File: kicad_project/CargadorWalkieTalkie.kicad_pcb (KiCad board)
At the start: 2 copper layers, 9 parts, among them J1 Screw_Terminal_01x02, J2 Screw_Terminal_01x02

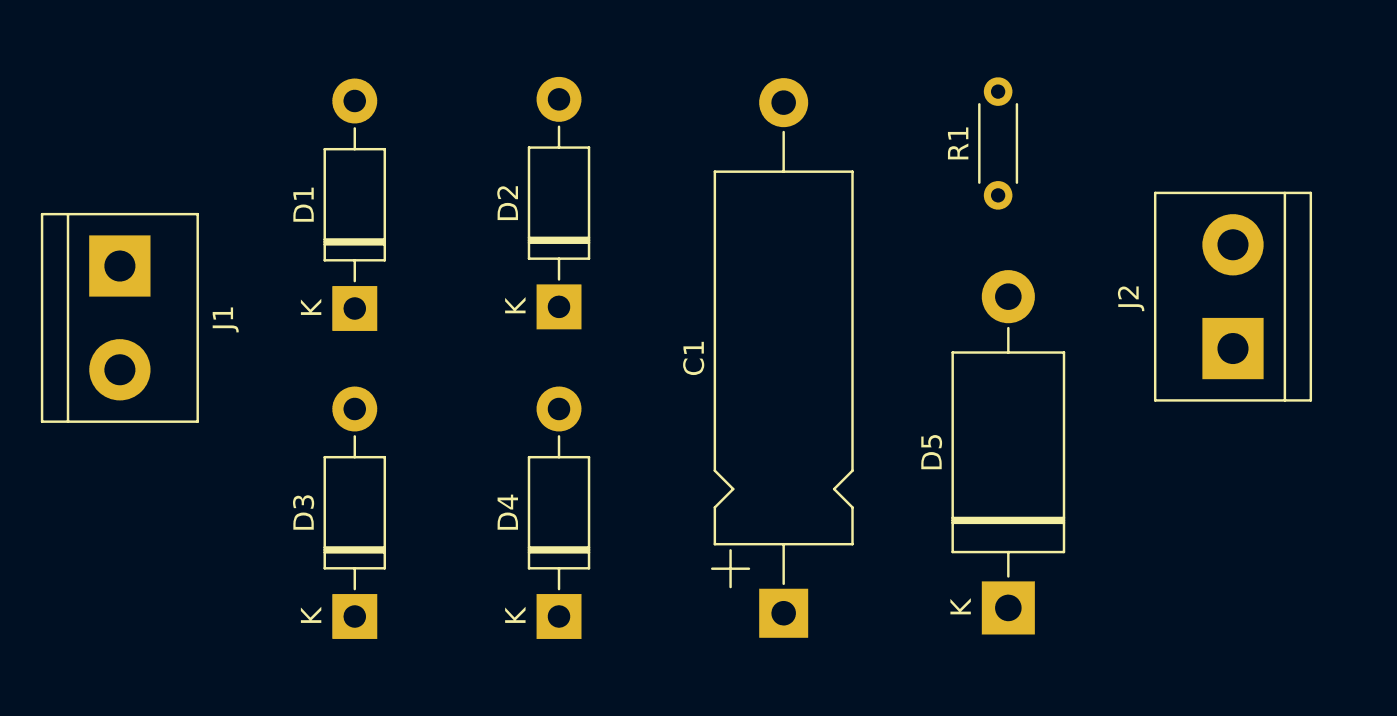
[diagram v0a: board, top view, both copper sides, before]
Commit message: Agregando las capas y enrutamiento en las capas de la PCB
Signed-off-by: RoMadrigal <rmadrigalmontes@gmail.com>
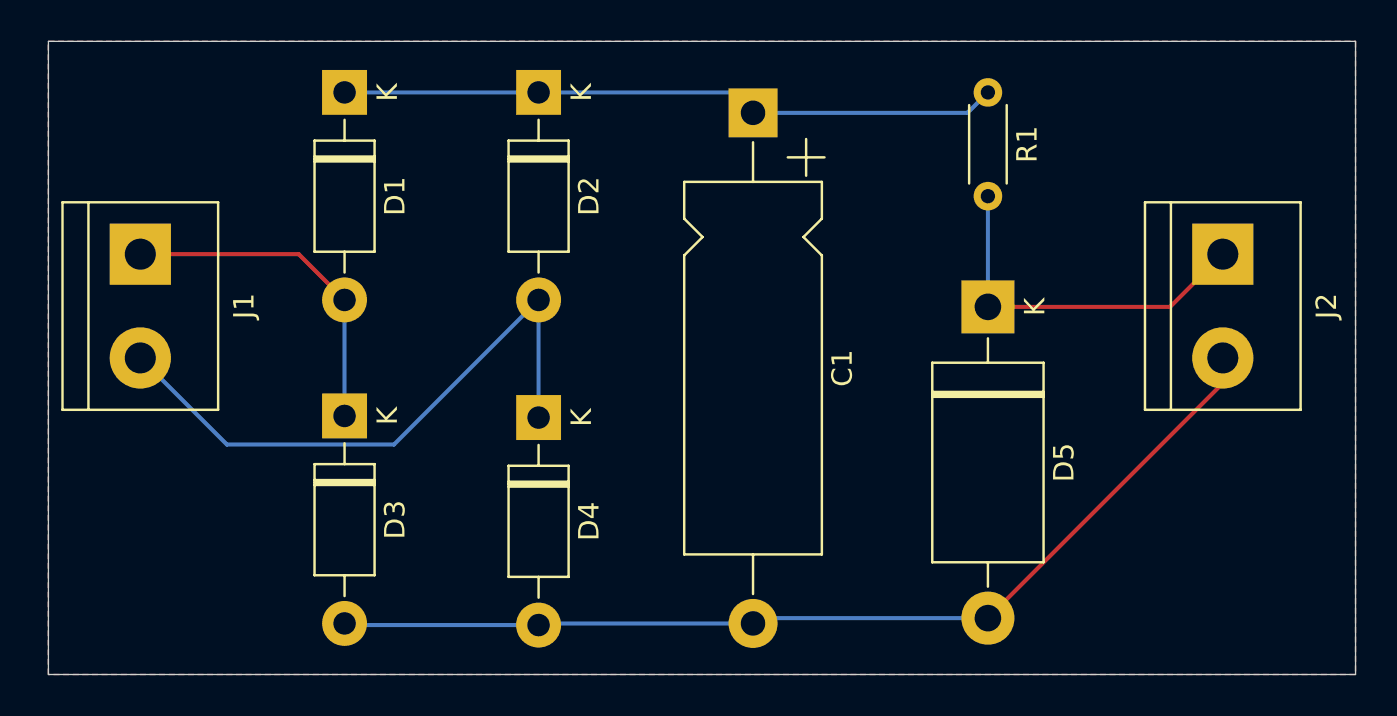
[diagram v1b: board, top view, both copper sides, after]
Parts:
- D5: value 1N53xxB -> 1N5338B
- moved C1 24.5 mm to (125.5, 79.0), turned to -90 degrees
- moved D5 14.8 mm to (137.0, 88.5), turned to -90 degrees
- moved D1 10.6 mm to (105.5, 78.0), turned to -90 degrees
- moved D2 10.5 mm to (115.0, 78.0), turned to -90 degrees
- moved D3 9.83 mm to (105.5, 93.8), turned to -90 degrees
- moved D4 9.79 mm to (115.0, 93.9), turned to -90 degrees
- moved R1 5.06 mm to (137.0, 78.0), turned to -90 degrees
- moved J2 4.65 mm to (148.5, 85.9), turned to -90 degrees
- moved J1 1.16 mm to (95.5, 85.9)
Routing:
- net Net-(D3-A): track 0.00 -> 49.2 mm
- net Net-(D1-K): track 0.00 -> 32.3 mm
- net /gnd: track 0.00 -> 29.9 mm
- net Net-(D5-K): track 0.00 -> 18.0 mm
- net /Vs: track 0.00 -> 16.6 mm
- added copper zone on B.Cu, net /Vs
- added copper zone on F.Cu, net /gnd
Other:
- board outline added: 64 x 31 mm

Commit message: Agregando nombres de los integrantes y del proyecto en la PCB
Signed-off-by: RoMadrigal <rmadrigalmontes@gmail.com>
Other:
- board text added: "WT-Charger V1 Anthony Calvo García - C11433 Rodrigo Madrigal Montes - C24458"
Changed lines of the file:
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@@
 		(layer "Edge.Cuts")
+	)
+	(gr_text "WT-Charger V1\nAnthony Calvo García - C11433\nRodrigo Madrigal Montes - C24458\n"
+		(at 144 99 0)
+		(layer "B.SilkS")
+		(effects
+			(font
+				(size 1 1)
+				(thickness 0.1)
+			)
+			(justify left bottom mirror)
+		)
 	)
 	(segment
